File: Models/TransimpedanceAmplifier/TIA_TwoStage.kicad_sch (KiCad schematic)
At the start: 8 parts

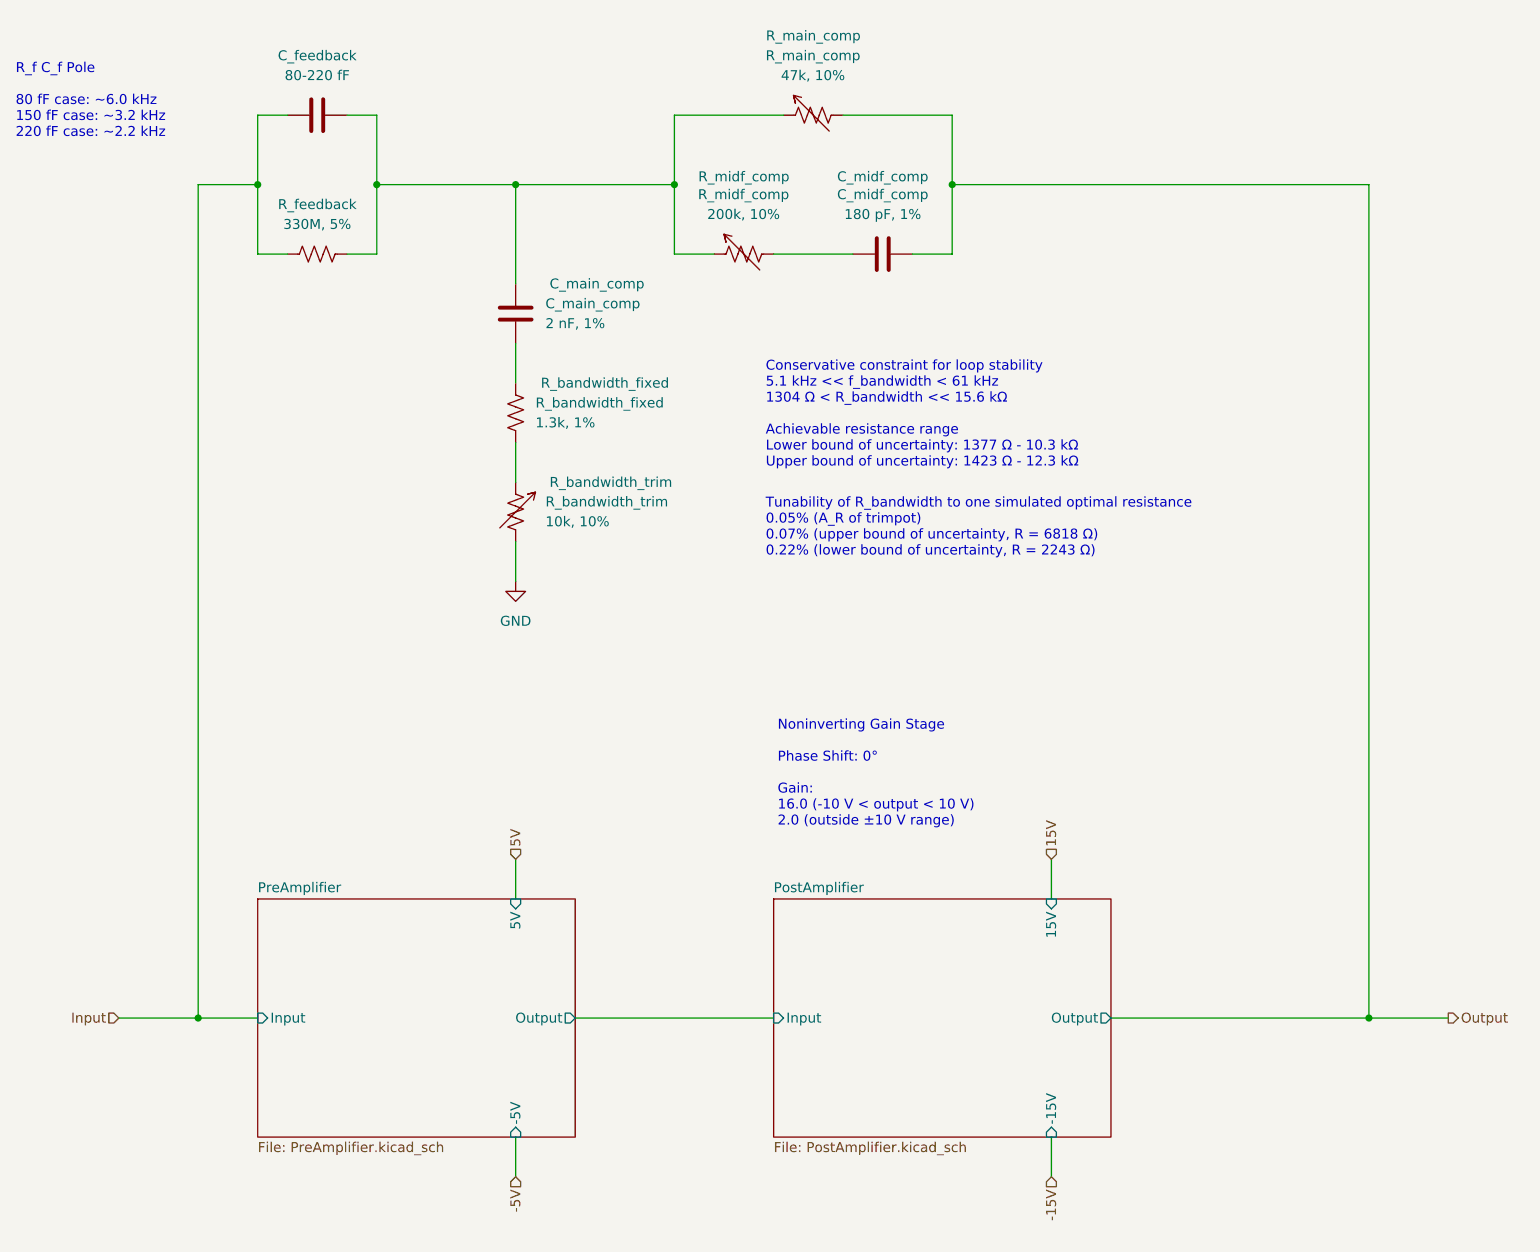
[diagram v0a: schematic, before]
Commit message: Overhauled all of the annotations
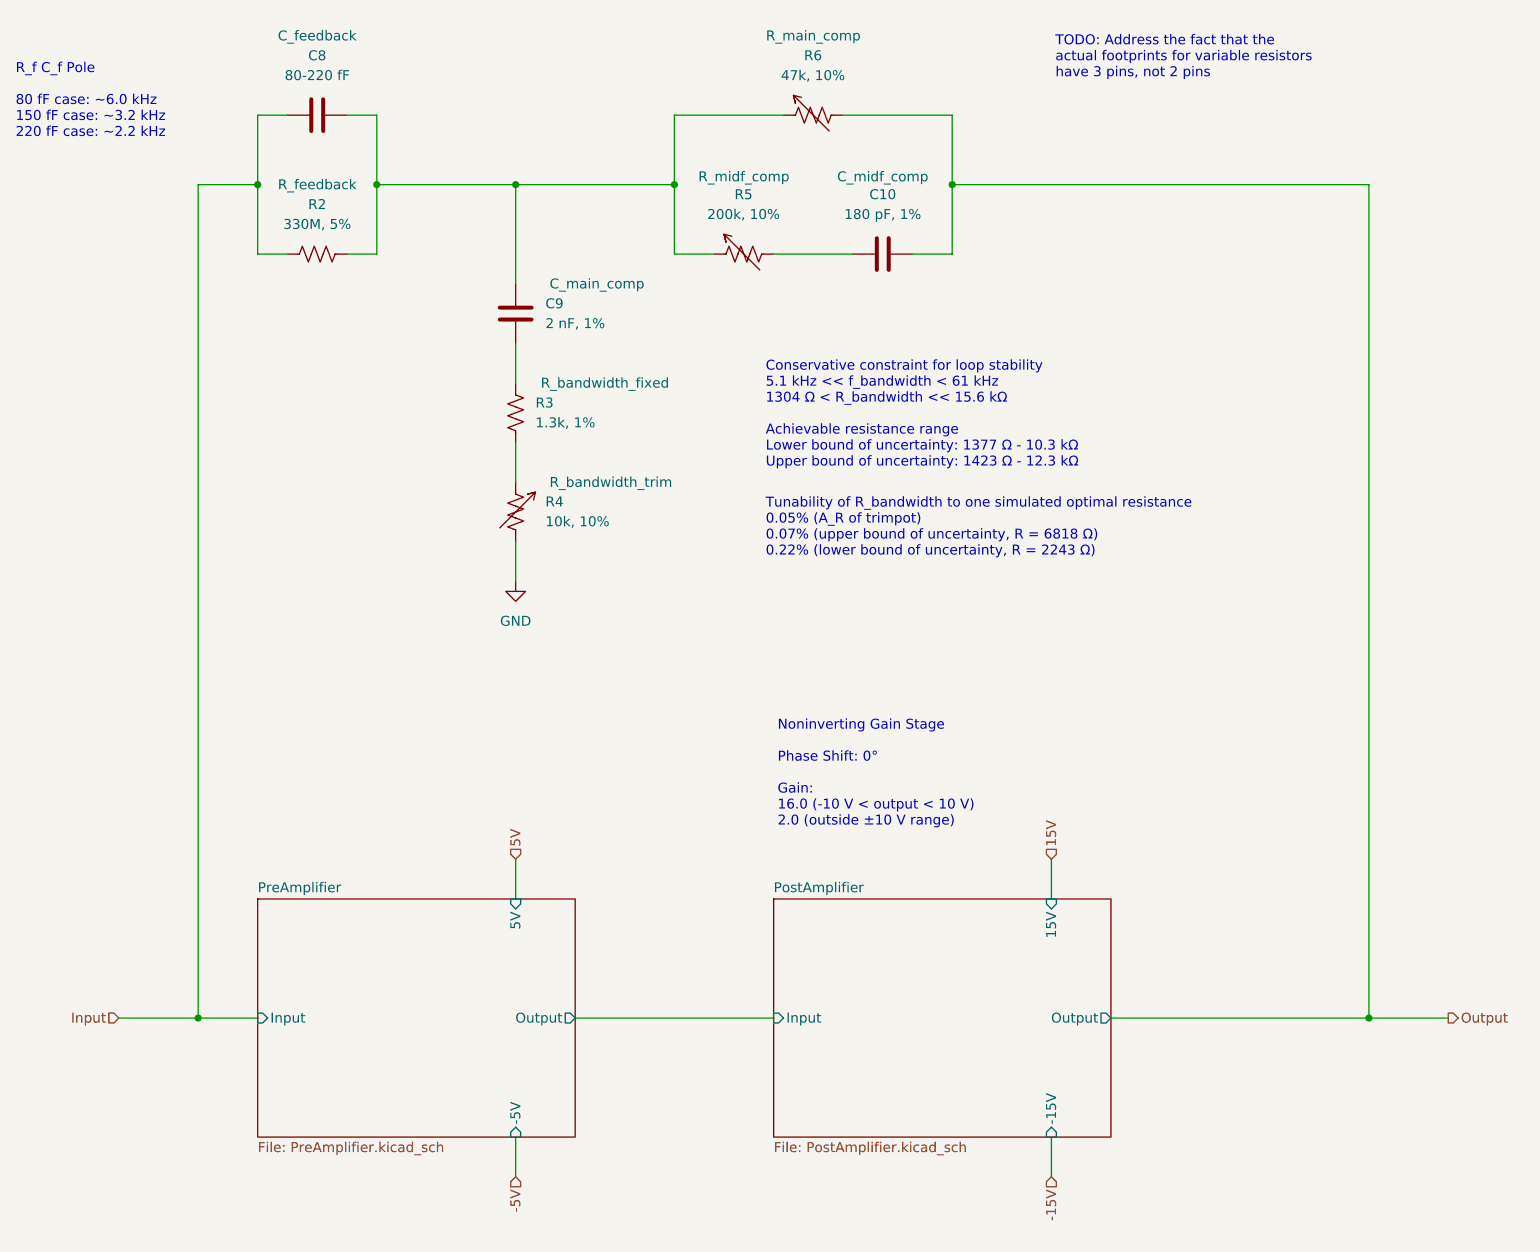
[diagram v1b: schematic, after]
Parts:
- renumbered C_midf_comp to C10, C_feedback to C8, C_main_comp to C9, R_feedback to R2, R_bandwidth_fixed to R3, R_bandwidth_trim to R4, R_midf_comp to R5, R_main_comp to R6
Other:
- note added: "TODO: Address the fact that the actual footprints for variable resistors have 3 pins, not 2 pins"
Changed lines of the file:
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@@
+		)
+	)
+	(text "TODO: Address the fact that the\nactual footprints for variable resistors\nhave 3 pins, not 2 pins"
+		(exclude_from_sim no)
+		(at 163.068 21.59 0)
+		(effects
+			(font
+				(size 1.27 1.27)
+			)
+			(justify left top)
 		)
 	)
@@
 		(on_board yes)
 		(dnp no)
-		(property "Reference" "C_main_comp"
+		(property "Reference" "C9"
 			(at 97.79 55.8799 0)
 			(effects
@@
 			(project ""
 				(path "/ec9f2ae3-e40d-40eb-9760-2b611ee8efd1/226b3d0c-9e45-4bcf-9bef-58938aee743e"
-					(reference "C_main_comp")
+					(reference "C9")
 					(unit 1)
 				)
@@
 		(on_board yes)
 		(dnp no)
-		(property "Reference" "R_bandwidth_fixed"
+		(property "Reference" "R3"
 			(at 96.52 68.5799 0)
 			(effects
@@
 			(project ""
 				(path "/ec9f2ae3-e40d-40eb-9760-2b611ee8efd1/226b3d0c-9e45-4bcf-9bef-58938aee743e"
-					(reference "R_bandwidth_fixed")
+					(reference "R3")
 					(unit 1)
 				)
@@
 		(on_board yes)
 		(dnp no)
-		(property "Reference" "R_main_comp"
+		(property "Reference" "R6"
 			(at 132.0419 24.13 90)
 			(effects
@@
 			(project ""
 				(path "/ec9f2ae3-e40d-40eb-9760-2b611ee8efd1/226b3d0c-9e45-4bcf-9bef-58938aee743e"
-					(reference "R_main_comp")
+					(reference "R6")
 					(unit 1)
 				)
@@
 		(on_board no)
 		(dnp no)
-		(fields_autoplaced yes)
-		(property "Reference" "C_feedback"
+		(property "Reference" "C8"
 			(at 68.58 24.13 90)
 			(effects
@@
 			)
 		)
-		(property "Description" "Unpolarized capacitor"
-			(at 68.58 31.75 0)
-			(effects
-				(font
-					(size 1.27 1.27)
-				)
-				(hide yes)
+		(property "Description" "C_feedback"
+			(at 68.58 21.59 90)
+			(effects
+				(font
+					(size 1.27 1.27)
+				)
 			)
 		)
@@
 			(project ""
 				(path "/ec9f2ae3-e40d-40eb-9760-2b611ee8efd1/226b3d0c-9e45-4bcf-9bef-58938aee743e"
-					(reference "C_feedback")
+					(reference "C8")
 					(unit 1)
 				)
@@
 		(on_board yes)
 		(dnp no)
-		(property "Reference" "R_midf_comp"
+		(property "Reference" "R5"
 			(at 123.1519 41.91 90)
 			(effects
@@
 			(project "TransimpedanceAmplifier"
 				(path "/ec9f2ae3-e40d-40eb-9760-2b611ee8efd1/226b3d0c-9e45-4bcf-9bef-58938aee743e"
-					(reference "R_midf_comp")
+					(reference "R5")
 					(unit 1)
 				)
@@
 		(on_board yes)
 		(dnp no)
-		(fields_autoplaced yes)
-		(property "Reference" "R_feedback"
+		(property "Reference" "R2"
 			(at 68.58 43.18 90)
 			(effects
@@
 			)
 		)
-		(property "Description" "Resistor, US symbol"
-			(at 68.58 49.53 0)
-			(effects
-				(font
-					(size 1.27 1.27)
-				)
-				(hide yes)
+		(property "Description" "R_feedback"
+			(at 68.58 40.64 90)
+			(effects
+				(font
+					(size 1.27 1.27)
+				)
 			)
 		)
@@
 			(project ""
 				(path "/ec9f2ae3-e40d-40eb-9760-2b611ee8efd1/226b3d0c-9e45-4bcf-9bef-58938aee743e"
-					(reference "R_feedback")
+					(reference "R2")
 					(unit 1)
 				)
@@
 		(on_board yes)
 		(dnp no)
-		(property "Reference" "C_midf_comp"
+		(property "Reference" "C10"
 			(at 140.97 41.91 90)
 			(effects
@@
 			(project ""
 				(path "/ec9f2ae3-e40d-40eb-9760-2b611ee8efd1/226b3d0c-9e45-4bcf-9bef-58938aee743e"
-					(reference "C_midf_comp")
+					(reference "C10")
 					(unit 1)
 				)
@@
 		(dnp no)
 		(fields_autoplaced yes)
-		(property "Reference" "#PWR06"
+		(property "Reference" "#PWR015"
 			(at 93.98 97.79 0)
 			(effects
@@
 			(project ""
 				(path "/ec9f2ae3-e40d-40eb-9760-2b611ee8efd1/226b3d0c-9e45-4bcf-9bef-58938aee743e"
-					(reference "#PWR06")
+					(reference "#PWR015")
 					(unit 1)
 				)
@@
 		(on_board yes)
 		(dnp no)
-		(property "Reference" "R_bandwidth_trim"
+		(property "Reference" "R4"
 			(at 97.79 81.2418 0)
 			(effects
@@
 			(project "TransimpedanceAmplifier"
 				(path "/ec9f2ae3-e40d-40eb-9760-2b611ee8efd1/226b3d0c-9e45-4bcf-9bef-58938aee743e"
-					(reference "R_bandwidth_trim")
+					(reference "R4")
 					(unit 1)
 				)

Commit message: Finalized the last detail of the schematic
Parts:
- removed R4: 10k, 10%, symbol Device:R_Variable_US
- removed R5: 200k, 10%, symbol Device:R_Variable_US
- removed R6: 47k, 10%, symbol Device:R_Variable_US
- added R5: 10k, 10%, symbol Device:R_Potentiometer_US
- added R6: 200k, 10%, symbol Device:R_Potentiometer_US
- added R7: 47k, 10%, symbol Device:R_Potentiometer_US
- renumbered R2 to R3, R3 to R4
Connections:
- net GND: now also R5.1, R5.2
- net Output: now also R7.1, R7.2
- net at C8.2, C9.1, R3.2: now also R6.3, R7.3
- net at R4.2: now also R5.3
- net at C10.1: now also R6.1, R6.2
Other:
- note added: "TODO: (all trimpots) Flip the connection point of pin 2 based on which is more convenient for the physical layout on the PCB"
- note removed: "TODO: Address the fact that the actual footprints for variable resistors have 3 pins, not 2 pins"

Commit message: Working on filling in the last details of the schematics
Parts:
- C10, C9: footprint (none) -> TwoTerminal:CAPC0603; Cost (none) -> $0.00; RoHS Compliant (none) -> NO
- C8, R3, R4, R5, R6, R7: Cost (none) -> $0.00; RoHS Compliant (none) -> NO
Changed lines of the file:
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@@
 			)
 		)
-		(property "Footprint" ""
+		(property "Footprint" "TwoTerminal:CAPC0603"
 			(at 94.9452 60.96 0)
 			(effects
@@
 		)
 		(property "Purchase Link" "https://www.digikey.com/en/products/detail/murata-electronics/GCM1885C1H202FA16D/16033535"
+			(at 93.98 57.15 0)
+			(effects
+				(font
+					(size 1.27 1.27)
+				)
+				(hide yes)
+			)
+		)
+		(property "Cost" "$0.00"
+			(at 93.98 57.15 0)
+			(effects
+				(font
+					(size 1.27 1.27)
+				)
+				(hide yes)
+			)
+		)
+		(property "RoHS Compliant" "NO"
 			(at 93.98 57.15 0)
 			(effects
@@
 			)
 		)
+		(property "Cost" "$0.00"
+			(at 123.19 49.53 90)
+			(effects
+				(font
+					(size 1.27 1.27)
+				)
+				(hide yes)
+			)
+		)
+		(property "RoHS Compliant" "NO"
+			(at 123.19 49.53 90)
+			(effects
+				(font
+					(size 1.27 1.27)
+				)
+				(hide yes)
+			)
+		)
 		(pin "2"
 		)
@@
 			)
 		)
+		(property "Cost" "$0.00"
+			(at 93.98 69.85 0)
+			(effects
+				(font
+					(size 1.27 1.27)
+				)
+				(hide yes)
+			)
+		)
+		(property "RoHS Compliant" "NO"
+			(at 93.98 69.85 0)
+			(effects
+				(font
+					(size 1.27 1.27)
+				)
+				(hide yes)
+			)
+		)
 		(pin "1"
 		)
@@
 			)
 		)
+		(property "Cost" "$0.00"
+			(at 68.58 31.75 90)
+			(effects
+				(font
+					(size 1.27 1.27)
+				)
+				(hide yes)
+			)
+		)
+		(property "RoHS Compliant" "NO"
+			(at 68.58 31.75 90)
+			(effects
+				(font
+					(size 1.27 1.27)
+				)
+				(hide yes)
+			)
+		)
 		(pin "2"
 		)
@@
 			)
 		)
+		(property "Cost" "$0.00"
+			(at 68.58 49.53 90)
+			(effects
+				(font
+					(size 1.27 1.27)
+				)
+				(hide yes)
+			)
+		)
+		(property "RoHS Compliant" "NO"
+			(at 68.58 49.53 90)
+			(effects
+				(font
+					(size 1.27 1.27)
+				)
+				(hide yes)
+			)
+		)
 		(pin "1"
 		)
@@
 			)
 		)
+		(property "Cost" "$0.00"
+			(at 93.98 82.55 0)
+			(effects
+				(font
+					(size 1.27 1.27)
+				)
+				(hide yes)
+			)
+		)
+		(property "RoHS Compliant" "NO"
+			(at 93.98 82.55 0)
+			(effects
+				(font
+					(size 1.27 1.27)
+				)
+				(hide yes)
+			)
+		)
 		(pin "2"
 		)
@@
 			)
 		)
-		(property "Footprint" ""
+		(property "Footprint" "TwoTerminal:CAPC0603"
 			(at 144.78 48.5648 0)
 			(effects
@@
 		(property "Purchase Link" "https://www.digikey.com/en/products/detail/murata-electronics/GCM1885C2A181FA16D/7363158"
 			(at 140.97 49.53 0)
+			(effects
+				(font
+					(size 1.27 1.27)
+				)
+				(hide yes)
+			)
+		)
+		(property "Cost" "$0.00"
+			(at 140.97 49.53 90)
+			(effects
+				(font
+					(size 1.27 1.27)
+				)
+				(hide yes)
+			)
+		)
+		(property "RoHS Compliant" "NO"
+			(at 140.97 49.53 90)
 			(effects
 				(font
@@
 			(effects
 				(font
+					(size 1.27 1.27)
+				)
+				(hide yes)
+			)
+		)
+		(property "Cost" "$0.00"
+			(at 132.08 29.21 90)
+			(effects
+				(font
+					(size 1.27 1.27)
+				)
+				(hide yes)
+			)
+		)
+		(property "RoHS Compliant" "NO"
+			(at 132.08 29.21 90)
+			(effects
+				(font

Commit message: Fixed a bug in footprint assignment
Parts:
- R3: footprint (none) -> TwoTerminal:RESC0805
- R4: footprint (none) -> TwoTerminal:RESC0603
- R5, R6, R7: footprint (none) -> ThreeTerminal:Bourns_3296Y
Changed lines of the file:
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@@
 			)
 		)
-		(property "Footprint" ""
+		(property "Footprint" "ThreeTerminal:Bourns_3296Y"
 			(at 123.19 49.53 0)
 			(effects
@@
 			)
 		)
-		(property "Footprint" ""
+		(property "Footprint" "TwoTerminal:RESC0603"
 			(at 94.996 70.104 90)
 			(effects
@@
 			)
 		)
-		(property "Footprint" ""
+		(property "Footprint" "TwoTerminal:RESC0805"
 			(at 68.834 48.514 90)
 			(effects
@@
 			)
 		)
-		(property "Footprint" ""
+		(property "Footprint" "ThreeTerminal:Bourns_3296Y"
 			(at 93.98 82.55 0)
 			(effects
@@
 			)
 		)
-		(property "Footprint" ""
+		(property "Footprint" "ThreeTerminal:Bourns_3296Y"
 			(at 132.08 29.21 0)
 			(effects

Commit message: Save progress
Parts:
- C10: Cost $0.00 -> $0.14; Cost (qty10) (none) -> $0.078; RoHS Compliant NO -> YES
- C8: Cost $0.00 -> (none); RoHS Compliant NO -> (none)
- C9: Cost $0.00 -> $0.17; Cost (qty10) (none) -> $0.096; RoHS Compliant NO -> YES
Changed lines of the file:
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@@
 			)
 		)
-		(property "Cost" "$0.00"
+		(property "Cost" "$0.17"
 			(at 93.98 57.15 0)
 			(effects
@@
 			)
 		)
-		(property "RoHS Compliant" "NO"
+		(property "RoHS Compliant" "YES"
+			(at 93.98 57.15 0)
+			(effects
+				(font
+					(size 1.27 1.27)
+				)
+				(hide yes)
+			)
+		)
+		(property "Cost (qty10)" "$0.096"
 			(at 93.98 57.15 0)
 			(effects
@@
 			)
 		)
-		(property "Cost" "$0.00"
+		(property "Cost" ""
 			(at 68.58 31.75 90)
 			(effects
@@
 			)
 		)
-		(property "RoHS Compliant" "NO"
+		(property "RoHS Compliant" ""
 			(at 68.58 31.75 90)
 			(effects
@@
 			)
 		)
-		(property "Cost" "$0.00"
+		(property "Cost" "$0.14"
 			(at 140.97 49.53 90)
 			(effects
@@
 			)
 		)
-		(property "RoHS Compliant" "NO"
+		(property "RoHS Compliant" "YES"
 			(at 140.97 49.53 90)
 			(effects
+				(font
+					(size 1.27 1.27)
+				)
+				(hide yes)
+			)
+		)
+		(property "Cost (qty10)" "$0.078"
+			(at 140.97 49.53 90)
+			(effects

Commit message: Added important links regarding high-voltage electronics
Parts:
- R3: Cost $0.00 -> $0.38; Cost (qty10) (none) -> $0.213; RoHS Compliant NO -> YES
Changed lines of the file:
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@@
 			)
 		)
-		(property "Cost" "$0.00"
+		(property "Cost" "$0.38"
 			(at 68.58 49.53 90)
 			(effects
@@
 			)
 		)
-		(property "RoHS Compliant" "NO"
+		(property "RoHS Compliant" "YES"
 			(at 68.58 49.53 90)
 			(effects
+				(font
+					(size 1.27 1.27)
+				)
+				(hide yes)
+			)
+		)
+		(property "Cost (qty10)" "$0.213"
+			(at 68.58 49.53 90)
+			(effects

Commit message: Almost done with generating bill of materials
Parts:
- R4: Cost $0.00 -> $0.10; Cost (qty10) (none) -> $0.030; RoHS Compliant NO -> YES
- R5, R7: Cost $0.00 -> $2.05; Cost (qty10) (none) -> $1.732; RoHS Compliant NO -> YES
- R6: Cost $0.00 -> $2.47; Cost (qty10) (none) -> $2.078; RoHS Compliant NO -> YES
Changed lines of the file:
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@@
 			)
 		)
-		(property "Cost" "$0.00"
+		(property "Cost" "$2.47"
 			(at 123.19 49.53 90)
 			(effects
@@
 			)
 		)
-		(property "RoHS Compliant" "NO"
+		(property "RoHS Compliant" "YES"
+			(at 123.19 49.53 90)
+			(effects
+				(font
+					(size 1.27 1.27)
+				)
+				(hide yes)
+			)
+		)
+		(property "Cost (qty10)" "$2.078"
 			(at 123.19 49.53 90)
 			(effects
@@
 			)
 		)
-		(property "Cost" "$0.00"
+		(property "Cost" "$0.10"
 			(at 93.98 69.85 0)
 			(effects
@@
 			)
 		)
-		(property "RoHS Compliant" "NO"
+		(property "RoHS Compliant" "YES"
+			(at 93.98 69.85 0)
+			(effects
+				(font
+					(size 1.27 1.27)
+				)
+				(hide yes)
+			)
+		)
+		(property "Cost (qty10)" "$0.030"
 			(at 93.98 69.85 0)
 			(effects
@@
 			)
 		)
-		(property "Cost" "$0.00"
+		(property "Cost" "$2.05"
 			(at 93.98 82.55 0)
 			(effects
@@
 			)
 		)
-		(property "RoHS Compliant" "NO"
+		(property "RoHS Compliant" "YES"
+			(at 93.98 82.55 0)
+			(effects
+				(font
+					(size 1.27 1.27)
+				)
+				(hide yes)
+			)
+		)
+		(property "Cost (qty10)" "$1.732"
 			(at 93.98 82.55 0)
 			(effects
@@
 			)
 		)
-		(property "Cost" "$0.00"
+		(property "Cost" "$2.05"
 			(at 132.08 29.21 90)
 			(effects
@@
 			)
 		)
-		(property "RoHS Compliant" "NO"
+		(property "RoHS Compliant" "YES"
 			(at 132.08 29.21 90)
 			(effects
+				(font
+					(size 1.27 1.27)
+				)
+				(hide yes)
+			)
+		)
+		(property "Cost (qty10)" "$1.732"
+			(at 132.08 29.21 90)
+			(effects

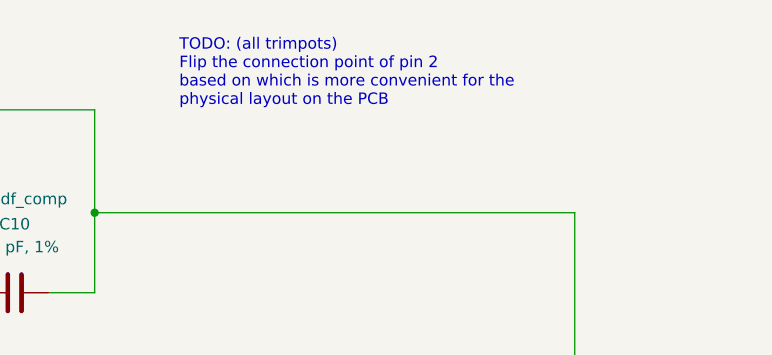
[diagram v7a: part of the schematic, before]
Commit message: Resolved the unknown about best wiring of trimpots for the pole-zero compensation network
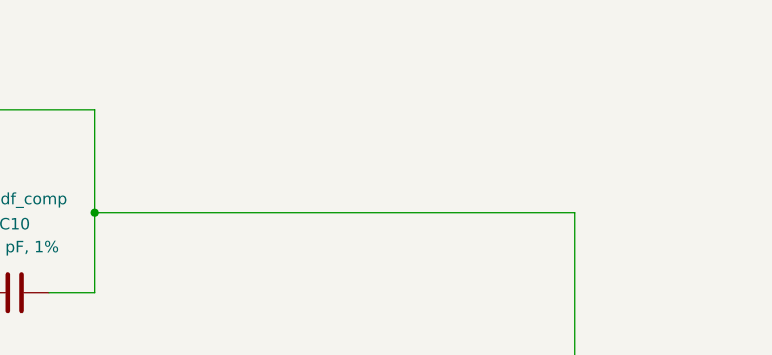
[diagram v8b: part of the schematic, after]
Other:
- note removed: "TODO: (all trimpots) Flip the connection point of pin 2 based on which is more convenient for the physical layout on the PCB"
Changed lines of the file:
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@@
-		)
-	)
-	(text "TODO: (all trimpots)\nFlip the connection point of pin 2\nbased on which is more convenient for the\nphysical layout on the PCB"
-		(exclude_from_sim no)
-		(at 159.258 21.336 0)
-		(effects
-			(font
-				(size 1.27 1.27)
-			)
-			(justify left top)
 		)
 	)
